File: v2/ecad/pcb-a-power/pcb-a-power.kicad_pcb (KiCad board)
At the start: 4 copper layers, 285 x 160 mm, 137 parts, among them U10 TPS2065CDBV, U11 INA219AIDCN, U12 USBLC6-2SC6, U13 TPS2065CDBV, U14 INA219AIDCN, U15 USBLC6-2SC6, U16 TPS2065CDBV, U17 INA219AIDCN, U18 USBLC6-2SC6, U19 PCA9555PW (0x21), U20 TPS61089 boost 5.05 V module 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, U5 AMS1117-3.3, U6 FE1.1s, U7 TPS2065CDBV, U8 INA219AIDCN, U9 USBLC6-2SC6, Y1 12 MHz 3225

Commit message: feat(release): A19, B12, E4 and E5 deliverables, all 0 hard and 0 unrouted; battery module model [MESHSAT-789] [MESHSAT-790] [MESHSAT-791]
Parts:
- removed F1: 15 A mini blade (Keystone 3568 holder): pack node to the X1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, Fuseholder_Blade_Mini_Keystone_3568
- removed JP1: BUSJ to GND = bus-powered, SolderJumper-2_P1.3mm_Open_RoundedPad1.0x1.5mm
- removed J_5V_MOD1: 5 V module rail to PCB-B J_5V_MOD (JST-VH, 18 AWG): + -, JST_VH_B2P-VH_1x02_P3.96mm_Vertical
- removed the J_DOCK at (138.0, 180.0)
- removed J_PACK: welded 1S8P pack, 8 x Samsung 35E, 1S BMS 15 A with NTC cut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, AMASS_XT60-M_1x02_P7.20mm_Vertical
- removed J_X1202BAT: lead to the X1202 battery terminals B+ / B- (holder solder 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, AMASS_XT60-M_1x02_P7.20mm_Vertical
- removed J_X1202DC: 12 V shore lead to the X1202 DC jack (XH2.5 -> 5521 plug), JST_XH_B2B-XH-A_1x02_P2.50mm_Vertical
- removed LED2: amber hub, LED_0603_1608Metric
- removed R45: 100k 1% (ILIM 10 A peak, 9 A min), R_0603_1608Metric
- removed R46: 17.4k, R_0603_1608Metric
- removed R49: 100k, R_0603_1608Metric
- removed R50: 10k, R_0603_1608Metric
- added C100: 100n, C_0603_1608Metric, F.Cu at (18.1, 85.2)
- added C101: 22u 10V X7R 1210, C_1210_3225Metric, F.Cu at (16.9, 104.0)
- added C102: 100n, C_0603_1608Metric, F.Cu at (132.3, 157.8)
- added C103: 10u, C_0805_2012Metric, F.Cu at (138.8, 151.6)
- added C104: 100n, C_0603_1608Metric, F.Cu at (67.0, 74.4)
- added C105: 100n, C_0603_1608Metric, F.Cu at (48.1, 77.9)
- added C106: 10u, C_0805_2012Metric, F.Cu at (54.1, 74.6)
- added C107: 100n, C_0603_1608Metric, F.Cu at (86.0, 47.1)
- added C108: 100n, C_0603_1608Metric, F.Cu at (107.9, 76.4)
- added C33: 10u, C_0805_2012Metric, F.Cu at (134.1, 151.6)
- added C50: 100u 10V, C_1206_3216Metric, F.Cu at (-7.08, 163.8)
- added C51: 10u 25V 1210, C_1210_3225Metric, F.Cu at (88.9, 158.2)
- added C52: 10u 25V 1210, C_1210_3225Metric, F.Cu at (94.8, 158.2)
- added C53: 10u 25V 1210, C_1210_3225Metric, F.Cu at (100.6, 158.2)
- added C54: 10u 25V 1210, C_1210_3225Metric, F.Cu at (106.5, 158.2)
- added C55: 10u 25V 1210, C_1210_3225Metric, F.Cu at (112.3, 158.2)
- added C56: 10u 25V 1210, C_1210_3225Metric, F.Cu at (88.9, 162.7)
- added C57: 10u 25V 1210, C_1210_3225Metric, F.Cu at (94.8, 162.7)
- added C58: 10u 25V 1210, C_1210_3225Metric, F.Cu at (88.9, 173.2)
- added C59: 10u 25V 1210, C_1210_3225Metric, F.Cu at (94.8, 173.2)
- added C60: 10u 25V 1210, C_1210_3225Metric, F.Cu at (100.6, 173.2)
- added C61: 10u, C_0805_2012Metric, F.Cu at (105.9, 172.6)
- added C62: 10u, C_0805_2012Metric, F.Cu at (110.5, 172.6)
- added C63: 47n, C_0603_1608Metric, F.Cu at (99.8, 161.8)
- added C64: 47n, C_0603_1608Metric, F.Cu at (88.1, 176.8)
- added C65: 4.7u, C_0805_2012Metric, F.Cu at (115.2, 172.6)
- added C66: 1n, C_0603_1608Metric, F.Cu at (92.3, 176.8)
- added C67: 100n, C_0603_1608Metric, F.Cu at (96.5, 176.8)
- added C68: 100n, C_0603_1608Metric, F.Cu at (22.3, 167.4)
- added C69: 1u, C_0603_1608Metric, F.Cu at (2.10, 172.5)
- added C70: 22u 10V X7R 1210, C_1210_3225Metric, F.Cu at (16.8, 121.1)
- added C71: 100n 25V, C_0603_1608Metric, F.Cu at (22.1, 141.4)
- added C72: 2.2u, C_0603_1608Metric, F.Cu at (26.3, 141.4)
- added C73: 3.3n, C_0603_1608Metric, F.Cu at (34.7, 141.4)
- added C74: 27p, C_0603_1608Metric, F.Cu at (22.1, 144.1)
- added C75: 22u 10V X7R 1210, C_1210_3225Metric, F.Cu at (22.9, 124.2)
- added C76: 22u 10V X7R 1210, C_1210_3225Metric, F.Cu at (22.9, 128.7)
- added C77: 100n, C_0603_1608Metric, F.Cu at (22.1, 132.3)
- added C78: 22u 10V X7R 1210, C_1210_3225Metric, F.Cu at (42.9, 112.2)
- added C79: 22u 10V X7R 1210, C_1210_3225Metric, F.Cu at (48.8, 112.2)
- added C80: 22u 10V X7R 1210, C_1210_3225Metric, F.Cu at (42.9, 116.7)
- added C81: 22u 10V X7R 1210, C_1210_3225Metric, F.Cu at (48.8, 116.7)
- added C82: 22u 10V X7R 1210, C_1210_3225Metric, F.Cu at (42.9, 121.1)
- added C83: 22u 10V X7R 1210, C_1210_3225Metric, F.Cu at (48.8, 121.1)
- added C84: 100n 25V, C_0603_1608Metric, F.Cu at (54.1, 141.4)
- added C85: 2.2u, C_0603_1608Metric, F.Cu at (58.3, 141.4)
- added C86: 3.3n, C_0603_1608Metric, F.Cu at (66.7, 141.4)
- added C87: 27p, C_0603_1608Metric, F.Cu at (54.1, 144.1)
- added C88: 22u 10V X7R 1210, C_1210_3225Metric, F.Cu at (54.9, 124.2)
- added C89: 22u 10V X7R 1210, C_1210_3225Metric, F.Cu at (54.9, 128.7)
- added C90: 100n, C_0603_1608Metric, F.Cu at (54.1, 132.3)
- added C91: 22u 10V X7R 1210, C_1210_3225Metric, F.Cu at (74.9, 112.2)
- added C92: 22u 10V X7R 1210, C_1210_3225Metric, F.Cu at (80.8, 112.2)
- added C93: 22u 10V X7R 1210, C_1210_3225Metric, F.Cu at (74.9, 116.7)
- added C94: 22u 10V X7R 1210, C_1210_3225Metric, F.Cu at (80.8, 116.7)
- added C95: 100u 10V, C_1206_3216Metric, F.Cu at (10.9, 125.1)
- added C96: 100u 10V, C_1206_3216Metric, F.Cu at (42.9, 125.1)
- added C97: 100u 10V, C_1206_3216Metric, F.Cu at (74.9, 120.7)
- added C98: 1u, C_0603_1608Metric, F.Cu at (3.21, 94.4)
- added C99: 10n, C_0603_1608Metric, F.Cu at (25.3, 77.4)
- added F4: 10 A mini blade (Keystone 3568 holder): pack node to the M2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, Fuseholder_Blade_Mini_Keystone_3568, F.Cu at (20.0, 154.3)
- added F5: 15 A mini blade (Keystone 3568 holder): pack node to the Pi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, Fuseholder_Blade_Mini_Keystone_3568, F.Cu at (45.0, 154.3)
- added F6: 2.5A hold 30V 1812, Fuse_1812_4532Metric, F.Cu at (19.6, 78.6)
- added J_5V_M1: rail M1 to PCB-B J_5V_M1 (JST-VH, 18 AWG): + -, JST_VH_B2P-VH_1x02_P3.96mm_Vertical, F.Cu at (-1.76, 65.5)
- added J_5V_M2: rail M2 to PCB-B J_5V_M2 (JST-VH, 18 AWG): + -, JST_VH_B2P-VH_1x02_P3.96mm_Vertical, F.Cu at (13.2, 65.5)
- added J_5V_PI: Pi rail 5.1 V 5 A to PCB-B J_5V_PI (JST-VH, 18 AWG): + -, JST_VH_B2P-VH_1x02_P3.96mm_Vertical, F.Cu at (28.2, 65.5)
- added J_BM1: SMP-MAX slide-on receptacle R222M00720 (underside), UHF to 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, Radiall_SMPMAX_R222M00720, B.Cu at (50.0, 176.0)
- added J_BM2: SMP-MAX slide-on receptacle R222M00720 (underside), WIFI24 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, Radiall_SMPMAX_R222M00720, B.Cu at (66.0, 176.0)
- added J_BM3: SMP-MAX slide-on receptacle R222M00720 (underside), WIFI58 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, Radiall_SMPMAX_R222M00720, B.Cu at (124.0, 176.0)
- added J_BM4: SMP-MAX slide-on receptacle R222M00720 (underside), SDR to 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, Radiall_SMPMAX_R222M00720, B.Cu at (138.0, 176.0)
- added J_BM5: SMP-MAX slide-on receptacle R222M00720 (underside), LTE to 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, Radiall_SMPMAX_R222M00720, B.Cu at (220.0, 176.0)
- added J_BM6: SMP-MAX slide-on receptacle R222M00720 (underside), IRID to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, Radiall_SMPMAX_R222M00720, B.Cu at (242.0, 176.0)
- added J_BM7: SMP-MAX slide-on receptacle R222M00720 (underside), LORA to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, Radiall_SMPMAX_R222M00720, B.Cu at (253.0, 174.0)
- added J_CN1: 9 A spring pin, module return CELL_N (Mill-Max 0858 class, 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, Mill-Max_0858_power_pin, B.Cu at (3.00, 177.0)
- added J_CN2: 9 A spring pin, module return CELL_N (Mill-Max 0858 class, 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, Mill-Max_0858_power_pin, B.Cu at (7.00, 177.0)
- added J_CN3: 9 A spring pin, module return CELL_N (Mill-Max 0858 class, 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, Mill-Max_0858_power_pin, B.Cu at (11.0, 177.0)
- added J_CN4: 9 A spring pin, module return CELL_N (Mill-Max 0858 class, 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, Mill-Max_0858_power_pin, B.Cu at (15.0, 177.0)
- added J_CP1: 9 A spring pin, CELL+ (Mill-Max 0858 class, dock block), Mill-Max_0858_power_pin, B.Cu at (3.00, 183.0)
- added J_CP2: 9 A spring pin, CELL+ (Mill-Max 0858 class, dock block), Mill-Max_0858_power_pin, B.Cu at (7.00, 183.0)
- added J_CP3: 9 A spring pin, CELL+ (Mill-Max 0858 class, dock block), Mill-Max_0858_power_pin, B.Cu at (11.0, 183.0)
- added J_CP4: 9 A spring pin, CELL+ (Mill-Max 0858 class, dock block), Mill-Max_0858_power_pin, B.Cu at (15.0, 183.0)
- added J_DOCK: spring pins to the dock block (2x6, Preci-Dip 813-S1-012-10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, PogoPins_2x6, B.Cu at (26.0, 180.0)
- added J_HEAT: 12 V heating pad on the battery module (XH2.5): + -, JST_XH_B2B-XH-A_1x02_P2.50mm_Vertical, F.Cu at (-9.53, 83.2)
- added J_MAINSW: MAIN button lead from the panel (XH2.5): PB, GND, JST_XH_B2B-XH-A_1x02_P2.50mm_Vertical, F.Cu at (-9.53, 103.2)
- added J_PRE1: pre-charge pin, longer, mates first (32.24 AX), Mill-Max_0858_power_pin, B.Cu at (-1.00, 180.0)
- added J_RF1: SMA jack (Amphenol 132134, vertical), pigtail from the UHF 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, SMA_Amphenol_132134-11_Vertical, F.Cu at (50.0, 166.0)
- added J_RF2: SMA jack (Amphenol 132134, vertical), pigtail from the WIFI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, SMA_Amphenol_132134-11_Vertical, F.Cu at (66.0, 166.0)
- added J_RF3: SMA jack (Amphenol 132134, vertical), pigtail from the WIFI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, SMA_Amphenol_132134-11_Vertical, F.Cu at (124.0, 166.0)
- added J_RF4: SMA jack (Amphenol 132134, vertical), pigtail from the SDR 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, SMA_Amphenol_132134-11_Vertical, F.Cu at (138.0, 166.0)
- added J_RF5: SMA jack (Amphenol 132134, vertical), pigtail from the LTE 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, SMA_Amphenol_132134-11_Vertical, F.Cu at (220.0, 184.0)
- added J_RF6: SMA jack (Amphenol 132134, vertical), pigtail from the IRID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, SMA_Amphenol_132134-11_Vertical, F.Cu at (242.0, 184.0)
- added J_RF7: SMA jack (Amphenol 132134, vertical), pigtail from the LORA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, SMA_Amphenol_132134-11_Vertical, F.Cu at (257.0, 164.0)
- added J_WALL1: USB-A receptacle, internal cable to the Glenair 233-370 wal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, USB_A_Stewart_SS-52100-001_Horizontal, F.Cu at (-0.01, 44.5)
- added L3: 2.2uH XAL1010-222MED (Isat 34 A, 10 mm), L_Coilcraft_XAL1010-XXX, F.Cu at (34.0, 116.0)
- added L4: 2.2uH XAL1010-222MED (Isat 34 A, 10 mm), L_Coilcraft_XAL1010-XXX, F.Cu at (66.0, 116.0)
- added L5: 2.2uH XAL4030-222MEB (Isat 7.4 A) between SW1 and SW2 (750 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, L_Coilcraft_XAL4030-XXX, F.Cu at (110.0, 168.0)
- added L6: 3.3uH XAL4020-332MEB, L_Coilcraft_XAL4020-XXX, F.Cu at (8.00, 106.0)
- added Q5: 2N7002: Pi GPIO high = pull KILL low = power off, SOT-23, F.Cu at (-1.45, 95.3)
- added R51: 10R 2W 2512, R_2512_6332Metric, F.Cu at (4.46, 168.6)
- added R52: 3 mOhm 1% 3 W 2512 shunt (RALEC LR2512-23R003F4): gauge SRP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, R_2512_6332Metric, F.Cu at (30.0, 170.0)
- added R53: 4.7k 1% (PROG: 1S, 750 kHz), R_0603_1608Metric, F.Cu at (104.0, 161.8)
- added R54: 16.5k 1%, R_0603_1608Metric, F.Cu at (108.2, 161.8)
- added R55: 34.8k 1%, R_0603_1608Metric, F.Cu at (112.4, 161.8)
- added R56: 5.23k 1% (RT1 JEITA), R_0603_1608Metric, F.Cu at (116.6, 161.8)
- added R57: 30.1k 1% (RT2 JEITA), R_0603_1608Metric, F.Cu at (88.1, 166.3)
- added R58: 100k, R_0603_1608Metric, F.Cu at (92.3, 166.3)
- added R59: 10k, R_0603_1608Metric, F.Cu at (100.7, 176.8)
- added R60: 10k, R_0603_1608Metric, F.Cu at (104.9, 176.8)
- added R61: 8.87k, R_0603_1608Metric, F.Cu at (30.5, 141.4)
- added R62: 102k 1%, R_0603_1608Metric, F.Cu at (26.3, 144.1)
- added R63: 13.7k 1%, R_0603_1608Metric, F.Cu at (30.5, 144.1)
- added R64: 8.87k, R_0603_1608Metric, F.Cu at (62.5, 141.4)
- added R65: 75k 1%, R_0603_1608Metric, F.Cu at (58.3, 144.1)
- added R66: 10k 1%, R_0603_1608Metric, F.Cu at (62.5, 144.1)
- added R67: 100k, R_0603_1608Metric, F.Cu at (7.42, 94.4)
- added R68: 100k, R_0603_1608Metric, F.Cu at (11.6, 94.4)
- added R69: 100k, R_0603_1608Metric, F.Cu at (15.8, 94.4)
- added R70: 100k, R_0603_1608Metric, F.Cu at (-1.90, 99.0)
- added R71: 1.02k 1% (2.0 A), R_0603_1608Metric, F.Cu at (18.1, 82.5)
- added R72: 10k, R_0603_1608Metric, F.Cu at (22.3, 82.5)
- added R73: 100k, R_0603_1608Metric, F.Cu at (26.5, 82.5)
- added R74: 33.2k 1%, R_0603_1608Metric, F.Cu at (16.1, 107.6)
- added R75: 10k 1%, R_0603_1608Metric, F.Cu at (20.3, 107.6)
- added R76: 10k, R_0603_1608Metric, F.Cu at (58.6, 74.4)
- added R77: 100k, R_0603_1608Metric, F.Cu at (62.8, 74.4)
- added R78: 0.1R 1% 1206, R_1206_3216Metric, F.Cu at (48.9, 74.8)
- added R79: 10k, R_0603_1608Metric, F.Cu at (81.8, 47.1)
- added RT1: 10k NTC 0603 1% (gauge temperature, beside the dock pins; t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, R_0603_1608Metric, F.Cu at (6.32, 172.5)
- added TP14: DOCK_SPARE, TestPoint_Pad_D1.5mm, F.Cu at (-10.1, 76.1)
- added TP15: BOOST_EN, TestPoint_Pad_D1.5mm, F.Cu at (-6.38, 76.1)
- added TP16: CELL_SENSE_P, TestPoint_Pad_D1.5mm, F.Cu at (10.8, 167.9)
- added TP17: EXP_SP2, TestPoint_Pad_D1.5mm, F.Cu at (69.0, 34.9)
- added TP18: EXP_SP3, TestPoint_Pad_D1.5mm, F.Cu at (72.7, 34.9)
- added TP19: EXP2_SP0, TestPoint_Pad_D1.5mm, F.Cu at (73.9, 76.9)
- added TP20: EXP2_SP1, TestPoint_Pad_D1.5mm, F.Cu at (77.6, 76.9)
- added TP21: EXP2_SP2, TestPoint_Pad_D1.5mm, F.Cu at (81.4, 76.9)
- added TP22: EXP2_SP3, TestPoint_Pad_D1.5mm, F.Cu at (85.1, 76.9)
- added TP23: EXP2_SP4, TestPoint_Pad_D1.5mm, F.Cu at (88.9, 76.9)
- added TP24: EXP2_SP5, TestPoint_Pad_D1.5mm, F.Cu at (92.6, 76.9)
- added TP25: EXP2_SP6, TestPoint_Pad_D1.5mm, F.Cu at (96.4, 76.9)
- added TP26: EXP2_SP7, TestPoint_Pad_D1.5mm, F.Cu at (100.1, 76.9)
- added TP27: EXP2_SP8, TestPoint_Pad_D1.5mm, F.Cu at (103.9, 76.9)
- added TP28: AB_SPARE, TestPoint_Pad_D1.5mm, F.Cu at (150.5, 151.9)
- added U21: BQ34Z100-G1 gauge (I2C 0x55, SCALED for 42 Ah, 3 mOhm shunt), TSSOP-14_4.4x5mm_P0.65mm, F.Cu at (38.0, 170.1)
- added U22: TPS61288L boost +5V_M1 (15 A switch, 500 kHz, no MODE pin), Texas_RQQ0011A_VQFN-HR-11_2.5x3mm, F.Cu at (2.12, 130.0)
- added U23: TPS61288L boost +5V_M2 (15 A switch, 500 kHz, no MODE pin), Texas_RQQ0011A_VQFN-HR-11_2.5x3mm, F.Cu at (34.1, 130.0)
- added U24: TPS61288L boost +5V_PI (15 A switch, 500 kHz, no MODE pin), Texas_RQQ0011A_VQFN-HR-11_2.5x3mm, F.Cu at (66.1, 130.0)
- added U25: LTC2954CTS8-1 push-button on/off controller, TSOT-23-8, F.Cu at (0.00, 91.1)
- added U26: TPS259571DSGR eFuse 12 V 2.0 A for the heating pad, Texas_DSG0008A_WSON-8-1EP_2x2mm_P0.5mm_EP0.9x1.6mm, F.Cu at (10.0, 82.1)
- added U27: USBLC6-2SC6, SOT-23-6, F.Cu at (62.8, 37.1)
- added U28: TPS2065CDBV, SOT-23-5, F.Cu at (65.8, 67.5)
- added U29: INA219AIDCN, SOT-23-8, F.Cu at (58.8, 69.1)
- added U30: USBLC6-2SC6, SOT-23-6, F.Cu at (50.3, 69.1)
- added U31: PCA9555PW (0x24): wall port, heating pad, charger, gauge, TSSOP-24_4.4x7.8mm_P0.65mm, F.Cu at (105.2, 69.0)
- C13: value 100u 10V -> 100n; footprint C_1206_3216Metric -> C_0603_1608Metric
- C15: value 10u -> 22u 10V X7R 1210; footprint C_0805_2012Metric -> C_1210_3225Metric
- C16, C17: value 22p -> 27p
- C19, C21, C23: value 1u -> 100n
- C25, C27: value 10u -> 1u; footprint C_0805_2012Metric -> C_0603_1608Metric
- C26: value 100n -> 1u
- C39: value 1u -> 2.2u
- C40: value 4.7n -> 3.3n
- C41: value 22u 10V X7R 1210 -> 27p; footprint C_1210_3225Metric -> C_0603_1608Metric
- C43, C48: value 100n -> 22u 10V X7R 1210; footprint C_0603_1608Metric -> C_1210_3225Metric
- C44: value 22u 10V X7R 1210 -> 100n; footprint C_1210_3225Metric -> C_0603_1608Metric
- C49: value 100u 10V -> 22u 10V X7R 1210; footprint C_1206_3216Metric -> C_1210_3225Metric
- F3: value 15 A mini blade (Keystone 3568 holder): pack node to the 5 V module-rail boost -> 10 A mini blade (Keystone 3568 holder): pack node to the M1 converter
- L2: value 1.5uH XAL6030-152MEB (Isat 12 A, 5.6 mOhm) -> 2.2uH XAL1010-222MED (Isat 34 A, 10 mm); footprint L_Coilcraft_XAL6030-XXX -> L_Coilcraft_XAL1010-XXX
- R19: value 2.7k 1% (REXT, verify datasheet) -> 12.0k 1% (RBIAS)
- R25: value 1k -> 10k
- R44: value 301k 1% (500 kHz) -> 8.87k
- R47: value 63.4k 1% -> 102k 1%
- R48: value 20k 1% -> 13.7k 1%
- TP1: value +5V -> +5V_M1
- TP11: value EXP_SP3 -> CHG_INT
- TP12: value +5V_MOD -> +5V_M2
- TP13: value BOOST_CELL -> +5V_PI
- TP7: value EXP_SP2 -> GAUGE_ALERT
- U10, U13, U16, U7: footprint SOT-23-6 -> SOT-23-5
- U20: value TPS61089 boost 5.05 V module rail -> BQ25792 1S charger from SHORE_12V (3 A set over ILIM_HIZ, 750 kHz, I2C 0x6B); footprint Texas_VQFN-RNR0011A-11 -> Texas_RQM0029A_QFN-29_4x4mm
- U5: value AMS1117-3.3 -> TPS563201 3.3 V buck from M1; footprint SOT-223-3_TabPin2 -> SOT-23-6
- U6: value FE1.1s -> USB2517I-JZX seven-port USB 2.0 hub (strap defaults, ports 6-7 disabled); footprint SSOP-28_5.3x10.2mm_P0.65mm -> QFN-64-1EP_9x9mm_P0.5mm_EP4.7x4.7mm
- Y1: value 12 MHz 3225 -> 24 MHz 3225
- moved C27 168.1 mm to (56.5, 47.1)
- moved C26 162.5 mm to (52.3, 47.1)
- moved C7 157.7 mm to (-7.67, 167.2)
- moved R24 127.6 mm to (140.7, 157.8)
- moved C44 122.1 mm to (-9.89, 132.3)
- moved TP4 121.5 mm to (14.5, 167.9)
- moved TP5 121.5 mm to (18.3, 167.9)
- moved C32 121.0 mm to (140.7, 155.1)
- moved F3 118.0 mm to (-4.96, 154.3)
- moved C48 114.5 mm to (16.8, 116.7)
- moved C47 113.3 mm to (10.9, 116.7)
- moved C49 113.1 mm to (10.9, 121.1)
- moved C42 111.6 mm to (-9.07, 124.2)
- moved TP1 111.3 mm to (-10.1, 72.4)
- moved TP10 111.3 mm to (8.62, 72.4)
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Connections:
- C13 pad 1: +5V -> /BST33
- C13 pad 2: GND -> /SW33
- C14 pad 1: +5V -> /+5V_M1
- C18 pad 1: /HUB_VD33 -> +3V3
- C19 pad 1: /HUB_VD33 -> +3V3
- C20 pad 1: /HUB_VD18 -> +3V3
- C21 pad 1: /HUB_VD18 -> +3V3
- C22 pad 1: /+5V_MOD -> +3V3
- C23 pad 1: /HUB_RST -> +3V3
- C25 pad 1: /5V_WIFI -> /HUB_VD18
- C26 pad 1: +3V3 -> /HUB_VD18PLL
- C27 pad 1: /5V_GPS -> +3V3
- C29 pad 1: /5V_CODEC -> /5V_WIFI
- C31 pad 1: /5V_UART -> /5V_GPS
- C34 pad 1: /+5V_MOD -> /+5V_M1
- C35 pad 1: /+5V_MOD -> /+5V_M1
- C36 pad 1: /+5V_MOD -> /+5V_M1
- C37 pad 1: /+5V_MOD -> /+5V_M1
- C38 pad 1: /BOOT5 -> /BST1
- C38 pad 2: /SW5 -> /SW1
- C39 pad 1: /BST5_VCC -> /VCC1
- C40 pad 1: /COMP5C -> /COMP1C
- C41 pad 1: /BOOST_CELL -> /COMP1
- C42 pad 1: /BOOST_CELL -> /BOOST1_IN
- C43 pad 1: /BOOST_CELL -> /BOOST1_IN
- C44 pad 1: /+5V_MOD -> /BOOST1_IN
- C45 pad 1: /+5V_MOD -> /+5V_M1
- C46 pad 1: /+5V_MOD -> /+5V_M1
- C47 pad 1: /+5V_MOD -> /+5V_M1
- C48 pad 1: /+5V_MOD -> /+5V_M1
- C49 pad 1: /+5V_MOD -> /+5V_M1
- D2 pad 1: +5V -> /+5V_M1
- F3 pad 2: /BOOST_CELL -> /BOOST1_IN
- J_AB1 pad 1: +5V -> /PI_SHDN_REQ
- J_AB1 pad 12: /X1202_5V -> /AB_SPARE
- J_AB1 pad 2: +5V -> /PI_KILL
- L2 pad 1: /BOOST_CELL -> /BOOST1_IN
- L2 pad 2: /SW5 -> /SW1
- R18 pad 1: /+5V_MOD -> /+5V_M1
- R19 pad 1: /HUB_REXT -> /HUB_RBIAS
- R20 pad 1: /HUB_RST -> /HUB_CFG0
- R20 pad 2: /HUB_VD33 -> GND
- R21 pad 1: /HUB_BUSJ -> /HUB_CFG1
- R21 pad 2: /HUB_VD33 -> GND
- R22 pad 1: /HUB_TESTJ -> /HUB_DIS6M
- R22 pad 2: /HUB_VD33 -> +3V3
- R23 pad 1: /HUB_OVCJ -> /HUB_DIS6P
- R23 pad 2: /HUB_VD33 -> +3V3
- R24 pad 2: /HUB_VBUSM -> GND
- R25 pad 1: /HUB_VD33 -> /HUB_DIS7M
- R25 pad 2: /LED_HUB_A -> +3V3
- R44 pad 1: /FSW5 -> /COMP1
- R44 pad 2: /SW5 -> /COMP1C
- R47 pad 1: /+5V_MOD -> /+5V_M1
- R47 pad 2: /FB5 -> /FB1
- R48 pad 1: /FB5 -> /FB1
- TP1 pad 1: +5V -> /+5V_M1
- TP11 pad 1: /EXP_SP3 -> /CHG_INT
- TP12 pad 1: /+5V_MOD -> /+5V_M2
- TP13 pad 1: /BOOST_CELL -> /+5V_PI
- TP7 pad 1: /EXP_SP2 -> /GAUGE_ALERT
- U10 pad 5: /+5V_MOD -> /+5V_M1
- U13 pad 5: /+5V_MOD -> /+5V_M1
- U16 pad 5: /+5V_MOD -> /+5V_M1
- U20 pad 1: /FSW5 -> /CHG_STAT
- U20 pad 10: /BOOT5 -> GND
- U20 pad 11: /SW5 -> GND
- U20 pad 2: /BST5_VCC -> /SHORE_12V
- U20 pad 3: /FB5 -> /SHORE_12V
- U20 pad 4: /COMP5 -> /BTST1
- U20 pad 5: GND -> /REGN
- U20 pad 6: /+5V_MOD -> (no net)
- U20 pad 7: /MOD_EN -> (no net)
- U20 pad 8: /ILIM5 -> /SHORE_12V
- U20 pad 9: /BOOST_CELL -> /SHORE_12V
- U5 pad 2: +3V3 -> /SW33
- U5 pad 3: +5V -> /+5V_M1
- U6 pad 1: GND -> /USB_WIFI_N
- U6 pad 10: /USB_WIFI_N -> +3V3
- U6 pad 11: /USB_WIFI_P -> /USB_WALL_N
- U6 pad 12: /HUB_VD18 -> /USB_WALL_P
- U6 pad 13: /HUB_VD33 -> GND
- U6 pad 14: /HUB_REXT -> (no net)
- U6 pad 15: /USB_A_N -> (no net)
- U6 pad 16: /USB_A_P -> (no net)
- U6 pad 17: /HUB_RST -> (no net)
- U6 pad 18: /HUB_VBUSM -> (no net)
- U6 pad 19: /HUB_BUSJ -> GND
- U6 pad 2: /XOUT -> /USB_WIFI_P
- U6 pad 20: /+5V_MOD -> (no net)
- U6 pad 21: /HUB_VD33 -> /FLT_UART
- U6 pad 22: (no net) -> /FLT_CODEC
- U6 pad 23: /HUB_LED1 -> (no net)
- U6 pad 24: (no net) -> +3V3
- U6 pad 25: (no net) -> /HUB_VD18
- U6 pad 26: /HUB_OVCJ -> (no net)
- U6 pad 27: /HUB_TESTJ -> /FLT_GPS
- U6 pad 28: /HUB_VD18 -> /FLT_WIFI
- U6 pad 3: /XIN -> /USB_GPS_N
- U6 pad 4: /USB_UART_N -> /USB_GPS_P
- U6 pad 5: /USB_UART_P -> +3V3
- U6 pad 8: /USB_GPS_N -> /USB_UART_N
- U6 pad 9: /USB_GPS_P -> /USB_UART_P
- U7 pad 5: /+5V_MOD -> /+5V_M1
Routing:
- net GND: track 789.1 -> 1827.2 mm, vias 64 -> 146
- net /+5V_M1: track 0.00 -> 515.3 mm, vias 0 -> 12
- net /+5V_MOD: track 400.0 -> 0.00 mm, vias 9 -> 0
- net +3V3: track 443.4 -> 702.5 mm, vias 11 -> 24
- net /CHG_INT: track 0.00 -> 210.3 mm, vias 0 -> 5
- net /GAUGE_ALERT: track 0.00 -> 203.4 mm, vias 0 -> 5
- net /PI_SHDN_REQ: track 0.00 -> 166.9 mm, vias 0 -> 2
- net /+5V_PI: track 0.00 -> 157.0 mm, vias 0 -> 2
- net /+5V_M2: track 0.00 -> 142.2 mm, vias 0 -> 3
- net /BOOST_EN: track 0.00 -> 137.9 mm, vias 0 -> 5
- net /PI_KILL: track 0.00 -> 132.9 mm, vias 0 -> 2
- net /DOCK_SPARE: track 0.00 -> 132.2 mm, vias 0 -> 2
- net /SCL: track 359.8 -> 491.6 mm, vias 7 -> 12
- net /CELL_X: track 131.4 -> 0.00 mm
- net /EXP_SP2: track 152.9 -> 22.7 mm, vias 2 -> 0
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- added copper zone on In2.Cu, net +5V_M1
- added copper zone on B.Cu, net CELL+
- added copper zone on F.Cu, net CELL+
- added copper zone on B.Cu, net CELL_N
- added copper zone on F.Cu, net CELL_N
- added copper zone on In2.Cu, net GND
- removed copper zone on In2.Cu, net +5V_MOD
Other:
- outline, holes or cut-outs redrawn
- board text added: "BATTERY MODULE ON THE CASE FLOOR (32.22): 12 x Samsung 35E 1S12P 42 Ah, BMS 30 A, over the dock block pins"
- board text added: "BM IRIDIUM"
- board text added: "BM LORA"
- board text added: "BM LTE"
- board text added: "BM SDR"
- board text added: "BM UHF"
- board text added: "BM WIFI 2.4"
- board text added: "BM WIFI 5.8"
- board text added: "CHARGER ZONE (A19): BQ25792 from the dock 12 V into the node, JEITA on the module thermistor"
- board text added: "DOCK BLOCK (underside): J_DOCK 2x6 signal pins + 9 A power pins + pre-charge pin, land on the dock block"
- board text added: "HUB ZONE (A19): USB2517I seven-port hub, 5x eFuse + INA219 (WiFi GPS codec UART wall), PCA9555 0x21 + 0x24, LED drivers"
- board text added: "MAIN POWER CONTROL, HEATING PAD SWITCH, 3.3 V BUCK"
- board text added: "MESHSAT-709 / 789 | 285 x 160 x 1.6 mm FR-4, 4 layers | matte black | 2026-09-05"
- board text added: "PCB-A UNDERSIDE - 13.4 mm above the dock strip (32.21); dock block pins and seven SMP-MAX receptacles land on the dock"
- board text added: "POWER ZONE (A19): fuse row F3 F4 F5 F2 at Y -46, converters M1 M2 PI north of it, gauge by the pins"
- board text added: "SMA IRIDIUM"
- board text added: "SMA LORA"
- board text added: "SMA LTE"
- board text added: "SMA SDR"
- board text added: "SMA UHF"
- board text added: "SMA WIFI 2.4"
- board text added: "SMA WIFI 5.8"
- board text removed: "HUB ZONE (phase A2): 4-port USB 2.0 hub, 4x eFuse + INA219, PCA9555 0x21, LED drivers"
- board text removed: "MESHSAT-709 | 285 x 160 x 1.6 mm FR-4, 4 layers | matte black | 2026-09-04"
- board text removed: "PCB-A UNDERSIDE - 6 mm spacers on the dock strip; J_DOCK pins land on PCB-E1"
- board text removed: "PWR ZONE: 3.3 V LDO, test points; A17: F3 + TPS61089 5 V module-rail boost from the cell node, J_5V_MOD1 (VH) to PCB-B"
- board text removed: "WELDED PACK 1S8P (8x Samsung 35E, 130 x 74 x 18.5) -> J_PACK XT60 -> F1 -> J_X1202BAT lead; strap through the slots"

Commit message: feat(ecad): A19 rerouted on locked fine-pitch escapes (0 open, 0 hard), B12, E4 and E5 finished on real-net planes [MESHSAT-709] [MESHSAT-789]
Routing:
- net /SCL: track 491.6 -> 426.0 mm, vias 12 -> 13
- net /EN_UART: track 212.4 -> 183.8 mm
- net /FLT_CODEC: track 198.3 -> 170.0 mm, vias 5 -> 4
- net /EXP_INT: track 249.6 -> 222.2 mm
- net /PI_SHDN_REQ: track 166.9 -> 141.1 mm
- net /EN_CODEC: track 201.2 -> 176.5 mm, vias 5 -> 3
- net /LED_SYS_K: track 193.4 -> 170.9 mm, vias 2 -> 1
- net /SHORE_12V: track 231.0 -> 253.2 mm
- net /SDA: track 459.3 -> 437.6 mm, vias 16 -> 17
- net /USB_A_P: track 179.2 -> 200.3 mm, vias 3 -> 4
- net /LED_LTE_K: track 189.3 -> 168.2 mm, vias 2 -> 1
- net /FLT_UART: track 213.3 -> 193.4 mm, vias 6 -> 4
- net /MEZZ_CELL: track 94.2 -> 75.1 mm
- net /CHG_INT: track 210.3 -> 228.5 mm
- net /LED_MESH_A: track 148.3 -> 164.6 mm, vias 1 -> 2
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- added copper zone on In2.Cu, net /+5V_M1
- added copper zone on B.Cu, net /CELL+
- added copper zone on F.Cu, net /CELL+
- added copper zone on In2.Cu, net /CELL+
- added copper zone on B.Cu, net /CELL_N
- added copper zone on F.Cu, net /CELL_N
- removed copper zone on In2.Cu, net +5V_M1
- removed copper zone on B.Cu, net CELL+
- removed copper zone on F.Cu, net CELL+
- removed copper zone on In2.Cu, net CELL+
- removed copper zone on B.Cu, net CELL_N
- removed copper zone on F.Cu, net CELL_N

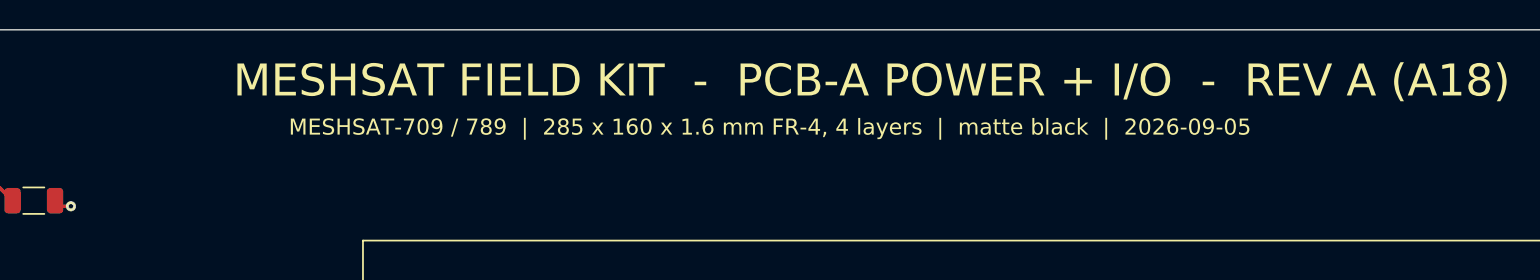
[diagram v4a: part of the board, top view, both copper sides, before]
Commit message: docs: date correction, every event of section 32.10 onward is 4 September 2026 (headers carry the commit clock, research notes renamed); superseded board folders moved under boards/superseded [MESHSAT-709]
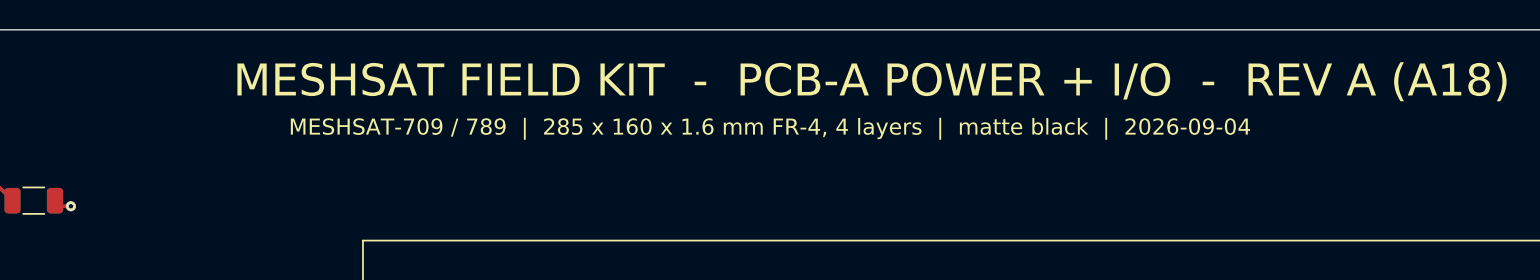
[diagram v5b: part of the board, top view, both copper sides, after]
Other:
- board text added: "MESHSAT-709 / 789 | 285 x 160 x 1.6 mm FR-4, 4 layers | matte black | 2026-09-04"
- board text removed: "MESHSAT-709 / 789 | 285 x 160 x 1.6 mm FR-4, 4 layers | matte black | 2026-09-05"
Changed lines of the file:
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@@
 		)
 	)
-	(gr_text "MESHSAT-709 / 789  |  285 x 160 x 1.6 mm FR-4, 4 layers  |  matte black  |  2026-09-05"
+	(gr_text "MESHSAT-709 / 789  |  285 x 160 x 1.6 mm FR-4, 4 layers  |  matte black  |  2026-09-04"
 		(at 198 36.7 0)
 		(layer "F.SilkS")

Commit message: feat(pcb-a,pcb-d): A20 and D6 routed and finished on the laptop [MESHSAT-795]
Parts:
- removed C102, C18, C19, C20, C21, C22, C23, C24, C28, C30, C32, C34, C35, C36, C37: 100n, C_0603_1608Metric
- removed C103, C29, C31, C33: 10u, C_0805_2012Metric
- removed C16, C17: 27p, C_0603_1608Metric
- removed C25, C26, C27: 1u, C_0603_1608Metric
- removed J_GPS1: USB-A receptacle, GPS, USB_A_Stewart_SS-52100-001_Horizontal
- removed J_WIFI1: USB-A receptacle, WiFi, USB_A_Stewart_SS-52100-001_Horizontal
- removed R19: 12.0k 1% (RBIAS), R_0603_1608Metric
- removed R20, R21, R22, R23, R25, R26, R28, R30, R32, R79: 10k, R_0603_1608Metric
- removed R24: 4.7k, R_0603_1608Metric
- removed R27, R29, R31, R33: 0.1R 1% 1206, R_1206_3216Metric
- removed R40, R41, R42, R43: 100k, R_0603_1608Metric
- removed S_GPS1, S_GPS2, S_GPS3, S_GPS4, S_WIFI1, S_WIFI2, S_WIFI3, S_WIFI4: tie slot, Slot_5x1.8_NPTH
- removed S_GPSC1, S_GPSC2, S_GPSC3: cable coil tie, Slot_5x1.8_NPTH
- removed TP28: AB_SPARE, TestPoint_Pad_D1.5mm
- removed U10, U13, U16, U7: TPS2065CDBV, SOT-23-5
- removed U11, U14, U17, U8: INA219AIDCN, SOT-23-8
- removed U12, U15, U18, U27, U9: USBLC6-2SC6, SOT-23-6
- removed U6: USB2517I-JZX seven-port USB 2.0 hub (strap defaults, ports 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, QFN-64-1EP_9x9mm_P0.5mm_EP4.7x4.7mm
- removed Y1: 24 MHz 3225, Crystal_SMD_3225-4Pin_3.2x2.5mm
- added TP29: EXP_SP4, TestPoint_Pad_D1.5mm, F.Cu at (67.9, 34.9)
- added TP30: EXP_SP5, TestPoint_Pad_D1.5mm, F.Cu at (71.7, 34.9)
- added TP31: EXP_SP6, TestPoint_Pad_D1.5mm, F.Cu at (75.4, 34.9)
- added TP32: EXP_SP7, TestPoint_Pad_D1.5mm, F.Cu at (79.2, 34.9)
- added TP33: EXP_SP8, TestPoint_Pad_D1.5mm, F.Cu at (82.9, 34.9)
- added TP34: EXP_SP9, TestPoint_Pad_D1.5mm, F.Cu at (86.7, 34.9)
- added TP35: EXP_SP10, TestPoint_Pad_D1.5mm, F.Cu at (90.4, 34.9)
- added TP36: EXP_SP11, TestPoint_Pad_D1.5mm, F.Cu at (94.2, 34.9)
- J_AB1: value A-B interconnect (IDC 2x7, top side) -> A-B interconnect (IDC 2x9, top side); footprint IDC-Header_2x07_P2.54mm_Vertical -> IDC-Header_2x09_P2.54mm_Vertical
- J_MEZZ1: value APRS mezzanine harness (IDC 2x8) -> APRS mezzanine harness (IDC 2x8): I2S and I2C for the D6 codec, its gated 3.3 V, PTT lines
- Q5: value 2N7002: Pi GPIO high = pull KILL low = power off -> 2N7002: Pi GPIO high = pull KILL low = power off (1 G, 2 S, 3 D; source and drain were swapped on A19, appendix 32.36)
- TP8: value MEZZ_SPARE1 -> I2S_DIN
- moved R38 58.9 mm to (48.1, 47.1)
- moved R39 22.5 mm to (135.6, 135.4)
- moved TP8 22.0 mm to (127.9, 135.9)
- moved TP9 22.0 mm to (131.6, 135.9)
- moved R34 17.6 mm to (102.3, 34.4)
- moved R36 17.6 mm to (110.8, 34.4)
- moved R37 17.6 mm to (115.0, 34.4)
- moved C107 17.6 mm to (98.1, 34.4)
- moved R35 17.6 mm to (106.5, 34.4)
- moved TP17 8.55 mm to (60.4, 34.9)
- moved TP18 8.55 mm to (64.2, 34.9)
- moved J_AB1 2.54 mm to (67.8, 183.8)
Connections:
- J_AB1 pad 11: /VBUS_A_SENSE -> /I2S_BCLK
- J_AB1 pad 12: /AB_SPARE -> /I2S_LRCLK
- J_AB1 pad 4: /USB_A_P -> /USB_WALL_P
- J_AB1 pad 5: /USB_A_N -> /USB_WALL_N
- J_MEZZ1 pad 14: /MEZZ_SPARE1 -> /SCL
- J_MEZZ1 pad 2: /5V_CODEC -> /+3V3_AB
- J_MEZZ1 pad 3: /USB_CODEC_P -> /I2S_BCLK
- J_MEZZ1 pad 4: /USB_CODEC_N -> /I2S_LRCLK
- J_MEZZ1 pad 6: /5V_UART -> /I2S_DOUT
- J_MEZZ1 pad 7: /USB_UART_P -> /I2S_DIN
- J_MEZZ1 pad 8: /USB_UART_N -> GND
- J_MEZZ1 pad 9: GND -> /SDA
- Q5 pad 2: /KILL -> GND
- Q5 pad 3: GND -> /KILL
- TP8 pad 1: /MEZZ_SPARE1 -> /I2S_DIN
- U19 pad 16: /FLT_WIFI -> /EXP_SP8
- U19 pad 17: /FLT_GPS -> /EXP_SP9
- U19 pad 18: /FLT_CODEC -> /EXP_SP10
- U19 pad 19: /FLT_UART -> /EXP_SP11
- U19 pad 4: /EN_WIFI -> /EXP_SP4
- U19 pad 5: /EN_GPS -> /EXP_SP5
- U19 pad 6: /EN_CODEC -> /EXP_SP6
- U19 pad 7: /EN_UART -> /EXP_SP7
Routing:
- net GND: track 1841.8 -> 150.2 mm, vias 149 -> 97
- net +3V3: track 708.8 -> 9.51 mm, vias 24 -> 5
- net /+5V_M1: track 506.1 -> 3.62 mm, vias 12 -> 2
- net /SDA: track 437.6 -> 12.3 mm, vias 17 -> 7
- net /SCL: track 426.0 -> 9.17 mm, vias 13 -> 5
- net /CELL+: track 342.1 -> 2.16 mm, vias 5 -> 2
- net /SHORE_12V: track 253.2 -> 3.35 mm, vias 7 -> 3
- net /CHG_INT: track 228.5 -> 1.64 mm, vias 5 -> 1
- net /EXP_INT: track 222.2 -> 4.68 mm, vias 3 -> 2
- net /EN_GPS: track 211.1 -> 0.00 mm, vias 3 -> 0
- net /FLT_GPS: track 209.2 -> 0.00 mm, vias 4 -> 0
- net /GAUGE_ALERT: track 211.1 -> 2.34 mm, vias 4 -> 1
- net /USB_GPS_N: track 203.8 -> 0.00 mm, vias 5 -> 0
- net /USB_A_P: track 200.3 -> 0.00 mm, vias 4 -> 0
- net /FLT_UART: track 193.4 -> 0.00 mm, vias 4 -> 0
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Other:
- board text added: "CONTROL ZONE (A20): wall-port eFuse + INA219, PCA9555 0x21 + 0x24, LED drivers (the hub went to B13)"
- board text added: "J_AB1 2x9 -> PCB-B underside (-72,-78)"
- board text added: "MESHSAT FIELD KIT - PCB-A POWER + I/O - REV A (A19)"
- board text removed: "ALFA AWUS036ACM 85 x 26 x 12 (MT7612U)"
- board text removed: "HUB ZONE (A19): USB2517I seven-port hub, 5x eFuse + INA219 (WiFi GPS codec UART wall), PCA9555 0x21 + 0x24, LED drivers"
- board text removed: "J_AB1 2x7 -> PCB-B underside (-72,-78)"
- board text removed: "J_GPS1"
- board text removed: "J_WIFI1"
- board text removed: "MESHSAT FIELD KIT - PCB-A POWER + I/O - REV A (A18)"
- board text removed: "USB-A 3.0 plug west -> J_WIFI1; 2x RP-SMA east -> WiFi bulkheads 1+2 (R16)"
- board text removed: "cable -> J_GPS1, coil on east slots"
- board text removed: "u-blox GPS puck 40 x 26 x 18"

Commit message: feat(pcb-a,pcb-d): A20 and D6 routed and finished (fix round) [MESHSAT-795]
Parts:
- moved J_LEDS1 6.00 mm to (100.8, 183.5)
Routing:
- net GND: track 150.2 -> 1441.6 mm, vias 97 -> 102
- net +3V3: track 9.51 -> 456.4 mm, vias 5 -> 6
- net /CELL+: track 2.16 -> 337.8 mm, vias 2 -> 6
- net /SCL: track 9.17 -> 338.2 mm, vias 5 -> 7
- net /SDA: track 12.3 -> 320.5 mm, vias 7 -> 8
- net /EXP_INT: track 4.68 -> 244.7 mm
- net /SHORE_12V: track 3.35 -> 241.7 mm, vias 3 -> 5
- net /+5V_M1: track 3.62 -> 221.4 mm, vias 2 -> 3
- net /GAUGE_ALERT: track 2.34 -> 209.5 mm, vias 1 -> 4
- net /LED_SYS_K: track 2.34 -> 208.3 mm, vias 1 -> 2
- net /CHG_INT: track 1.64 -> 203.1 mm, vias 1 -> 6
- net /LED_LTE_K: track 1.64 -> 198.9 mm, vias 1 -> 2
- net /LED_SAT_K: track 2.34 -> 199.3 mm, vias 1 -> 2
- net /LED_MESH_K: track 2.34 -> 198.1 mm, vias 1 -> 2
- net /LED_SYS_A: track 0.00 -> 192.9 mm, vias 0 -> 2
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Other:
- board text added: "MESHSAT FIELD KIT - PCB-A POWER + I/O - REV A (A18)"
- board text removed: "MESHSAT FIELD KIT - PCB-A POWER + I/O - REV A (A19)"
